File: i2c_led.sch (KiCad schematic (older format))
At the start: 20 parts, among them J1 Conn_01x04, J2 Conn_01x04, Q1 Q_NPN_BEC, Q2 BSS138, Q3 BSS138, U1 MCP4018-xxxxLT, U2 ME2188A50XG, U3 LMV321

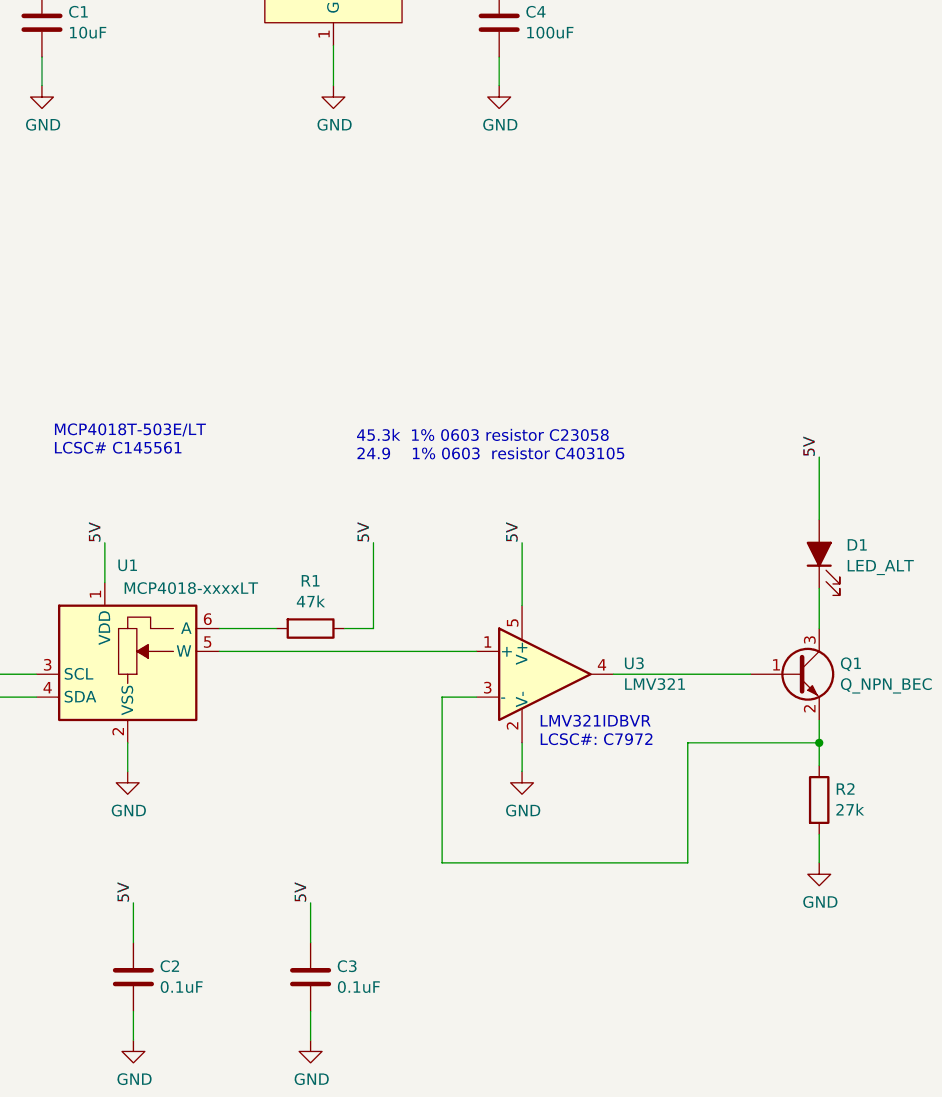
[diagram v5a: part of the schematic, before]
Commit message: Added notes about errors in design. Need to come back and fix them at some point.
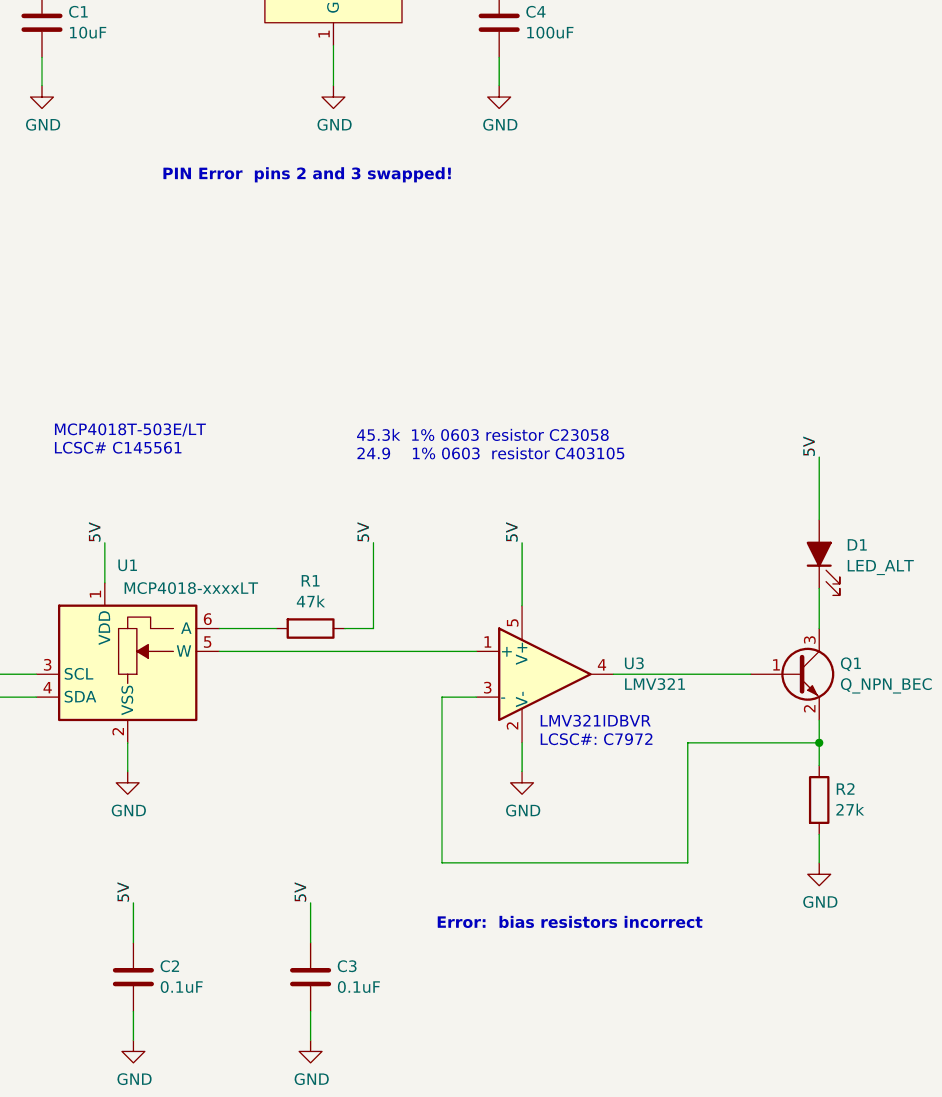
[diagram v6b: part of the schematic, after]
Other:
- note added: "Error: bias resistors incorrect"
- note added: "PIN Error pins 2 and 3 swapped!"
- note added: "\nDC-DC converter input 1.8-5V, output 5V\nLCSC Part# C236769\n"
- note removed: "\nDC-DC converter input 1.8-5V, output 5V\nLCSC Part# C236769"
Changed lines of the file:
@@
 Text Label 3850 1400 0    50   ~ 0
 5V
-Text Notes 1775 925  0    50   ~ 0
-\nDC-DC converter input 1.8-5V, output 5V\nLCSC Part# C236769
 $Comp
 L Connector_Generic:Conn_01x04 J1
@@
 	1    0    0    -1
 $EndComp
+Text Notes 1775 925  0    50   ~ 0
+\nDC-DC converter input 1.8-5V, output 5V\nLCSC Part# C236769\n
+Text Notes 2000 2425 0    50   ~ 10
+PIN Error  pins 2 and 3 swapped!
+Text Notes 3200 5700 0    50   ~ 10
+Error:  bias resistors incorrect
 $EndSCHEMATC
